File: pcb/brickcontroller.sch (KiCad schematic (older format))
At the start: 35 parts, among them J1 USB_C_Receptacle_USB2.0, J2 Conn_01x11_Male, J3 Conn_01x02, J4 Conn_01x02, Q1 SS8050, Q2 SS8050, SW1 SW_Push, U1 AMS1117-3.3, U2 SRV05-4, U3 CP2104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

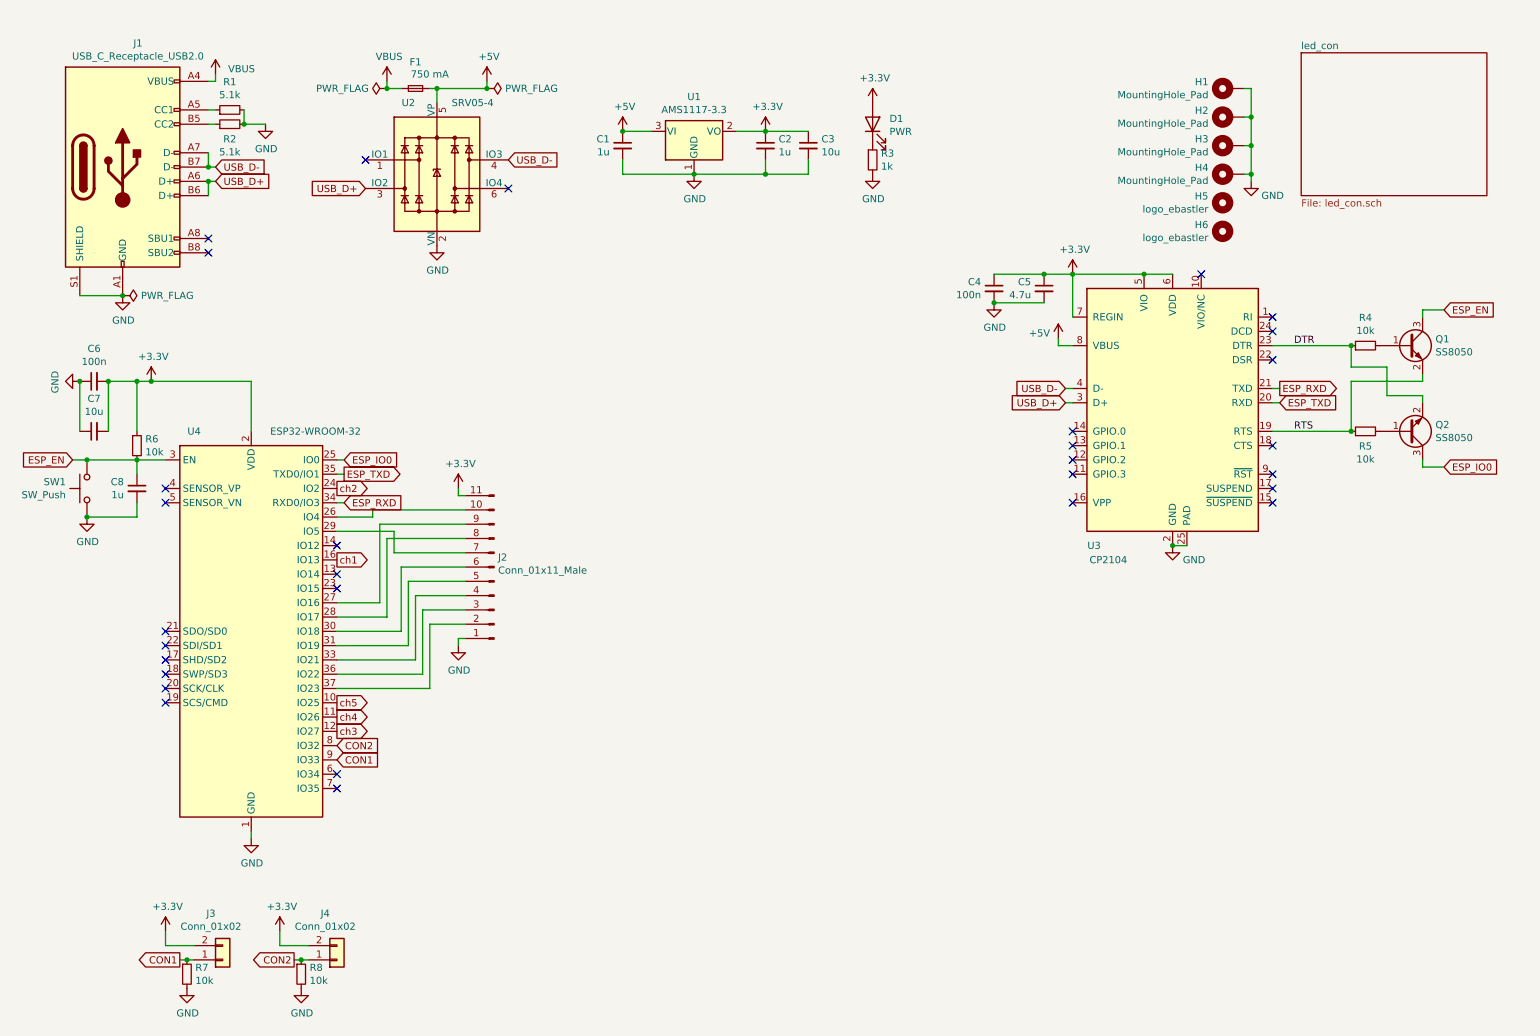
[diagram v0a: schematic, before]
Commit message: improved schematic readability
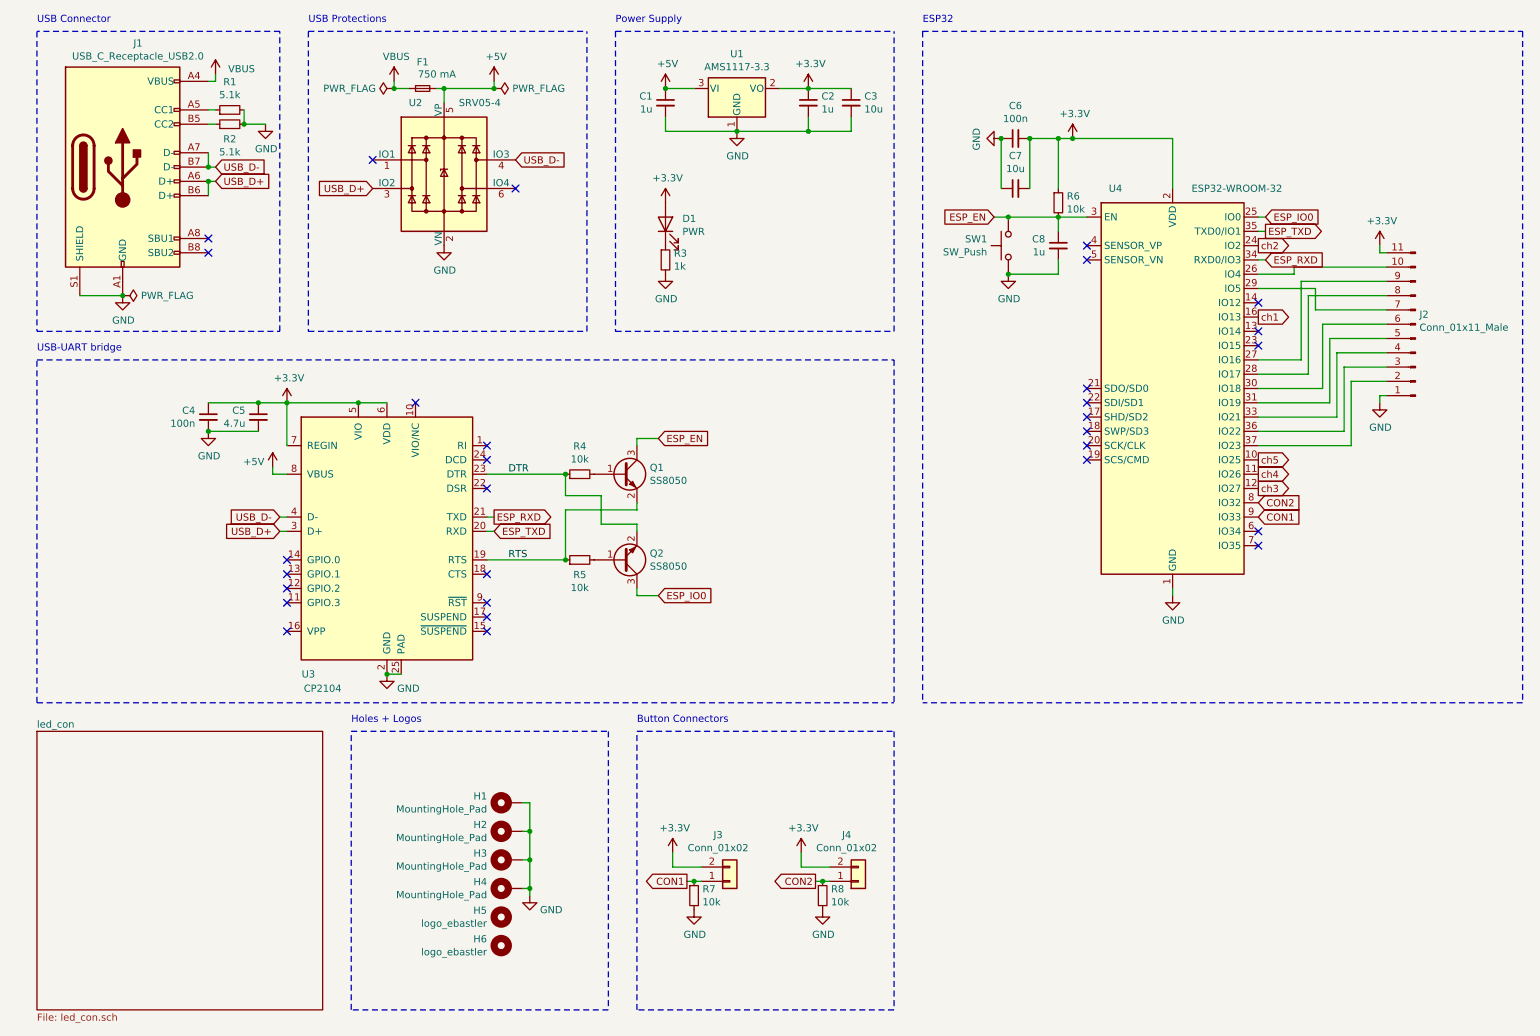
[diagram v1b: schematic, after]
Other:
- note added: "Button Connectors"
- note added: "ESP32"
- note added: "Holes + Logos"
- note added: "Power Supply"
- note added: "USB Connector"
- note added: "USB Protections"
- note added: "USB-UART bridge"
- moved on the sheet: C1, C2, C3, C4, C5, C6, C7, C8, D1, F1, H1, H2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
